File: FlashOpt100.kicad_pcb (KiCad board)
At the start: 2 copper layers, 16 x 38 mm, 8 parts, among them J1 Tandy_100_102_200_option_rom, J2 FlashOpt100_PRG_4x7, U1 29F010 TSOP

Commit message: cosmetics
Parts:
- R1, R2, R3: footprint 000_LOCAL:R_0805_2012Metric -> 000_LOCAL:R_0805
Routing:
- net GND: track 41.3 -> 41.4 mm, vias 3 -> 2

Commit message: update to v004 board outline and carrier
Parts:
- removed carrier?: pcb2molex8878_chamfer, 000_LOCAL:pcb2molex8878_chamfer
- J1: footprint 000_LOCAL:pcb2molex8878 -> 000_LOCAL:Molex78802_PCB_28
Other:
- board size 16 x 38 mm -> 16.6 x 38 mm
- board text added: "v004"

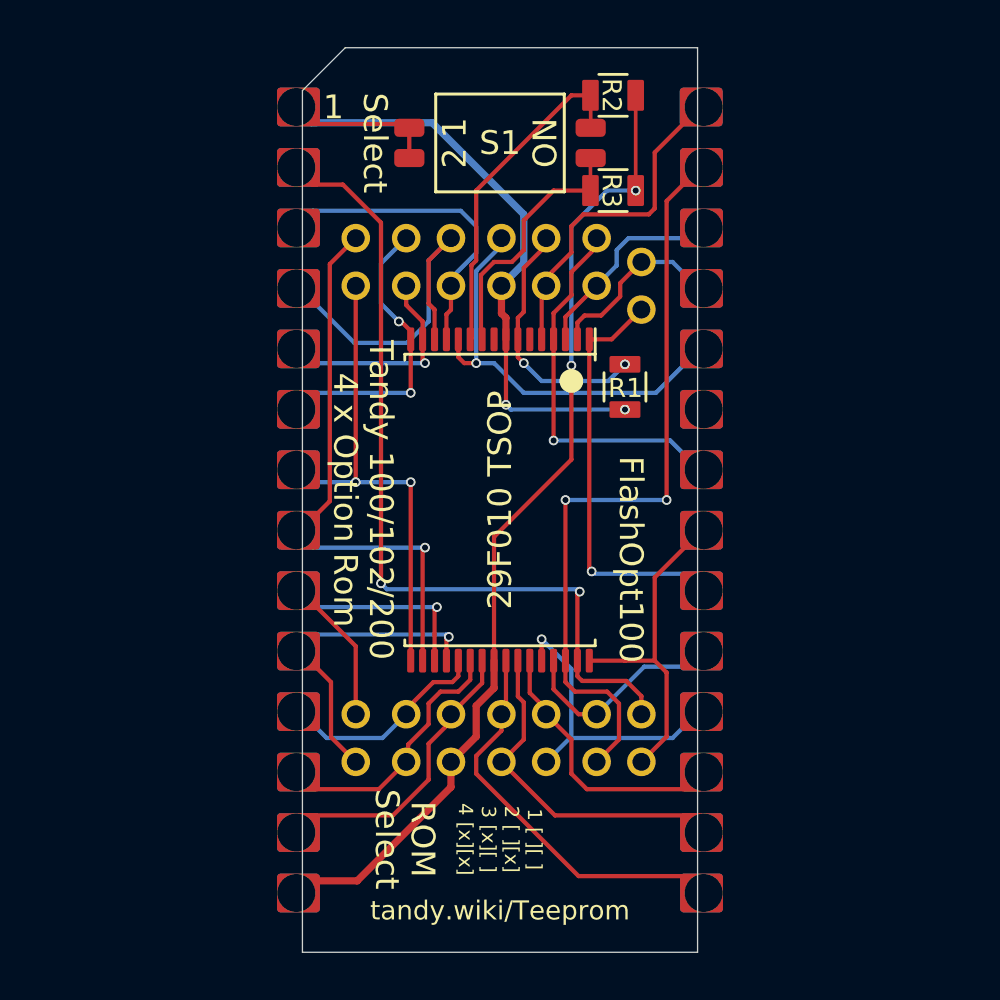
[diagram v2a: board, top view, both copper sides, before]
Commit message: kicad 6, flashopt100 programming socket
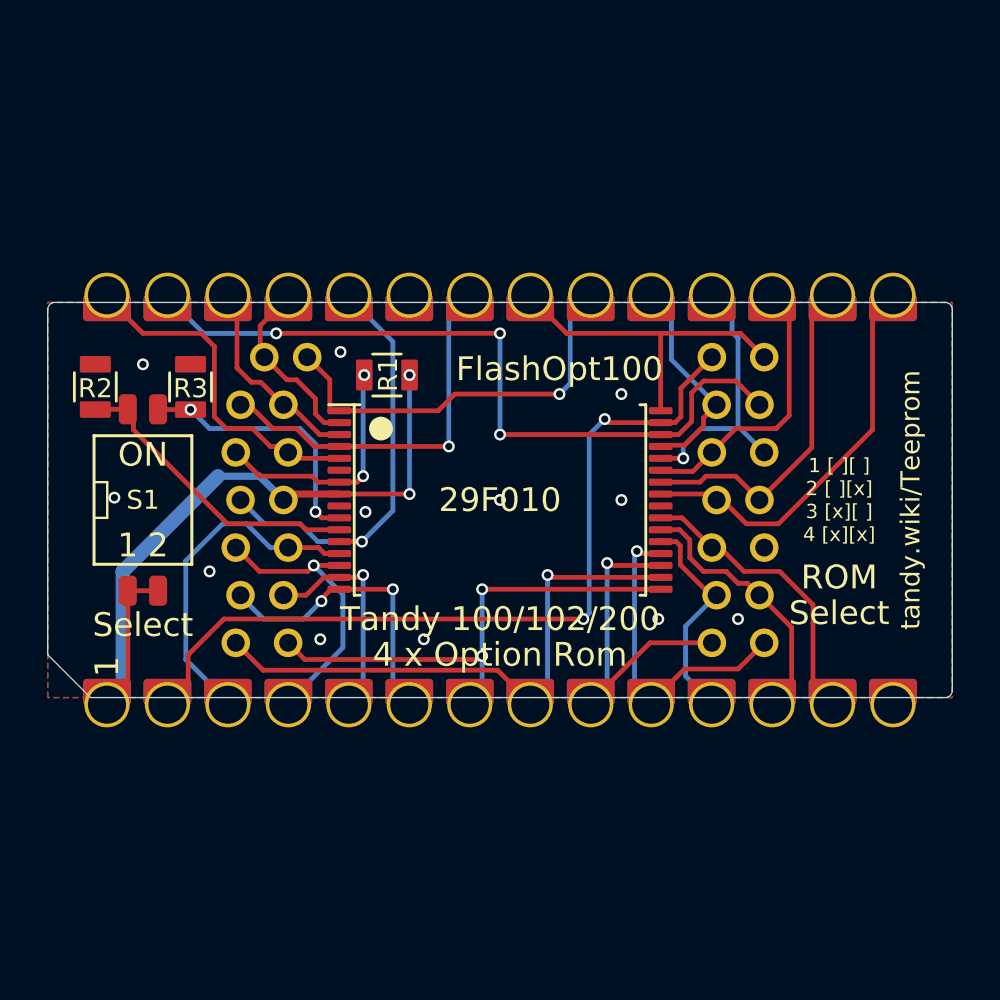
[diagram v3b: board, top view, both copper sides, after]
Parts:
- U1: value 29F010 TSOP -> 29F010
- moved R2 25.0 mm to (130.2, 94.4), turned to -90 degrees
- moved S1 21.2 mm to (132.2, 99.2), turned to 90 degrees
- moved R3 19.6 mm to (134.2, 94.4), turned to -90 degrees
- moved R1 10.0 mm to (142.5, 93.9), turned to 180 degrees
- turned J1 to 90 degrees
- turned J2 to 0 degrees
- turned U1 to -90 degrees
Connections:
- net /~CE renamed /~{CE}
- net /~OE renamed /~{OE}
- net /~WE renamed /~{WE}
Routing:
- net GND: track 41.4 -> 0.00 mm, vias 2 -> 12
- net /A6: track 15.6 -> 11.9 mm, vias 0 -> 1
- net /D6: track 13.1 -> 11.6 mm
- net /A15: track 14.2 -> 12.7 mm
- net /D4: track 15.8 -> 15.0 mm
- net /A10: track 35.6 -> 34.8 mm
- net /A7: track 13.4 -> 14.1 mm
- net /A8: track 8.73 -> 8.13 mm
- net /A1: track 14.9 -> 14.3 mm
- net /D1: track 11.7 -> 11.2 mm
- net /~{CE}: track 32.1 -> 31.6 mm, vias 2 -> 3
- net /A16: track 10.9 -> 11.2 mm, vias 0 -> 2
- added copper zone on B.Cu, net GND
- added copper zone on F.Cu, net GND
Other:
- board size 16.6 x 38 mm -> 38 x 16.6 mm
- net class Default removed
- board text added: "${COMMENT2}"
- board text added: "${TITLE} ${REVISION} ${COMMENT2}"
- board text added: "R1,R2,R3: ${00000000-0000-0000-0000-00005d22c129:VALUE}"
- board text added: "To program: Set bank with dip switches. Write 32K as 29C256."
- board text removed: "R1,R2,R3: 47k"
- board text removed: "tandy.wiki/Teeprom"
- board text removed: "v004"
